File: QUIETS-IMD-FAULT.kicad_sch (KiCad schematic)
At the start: 7 parts, among them K1 Relay_DPDT, K2 Relay_SPDT, K3 Relay_DPDT, Q1 NMOS

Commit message: Version 2
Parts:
- removed K3: Relay_DPDT, symbol Relay:Relay_DPDT
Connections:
- net +12V: no longer K1.11
- net GND: now also K1.11
- net IMD FAULT LIGHT: now also K1.22
- net IMD SAFETY RELAY: now reaches K1.14
- net RESET renamed IMD-RESET
- no-connect marks 3 -> 2
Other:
- note added: "Lors de l'activation du vehicule, il faut reset l'erreur pour activer le circuit"
- moved on the sheet: K1, K2, Q1, R1, R2, R3

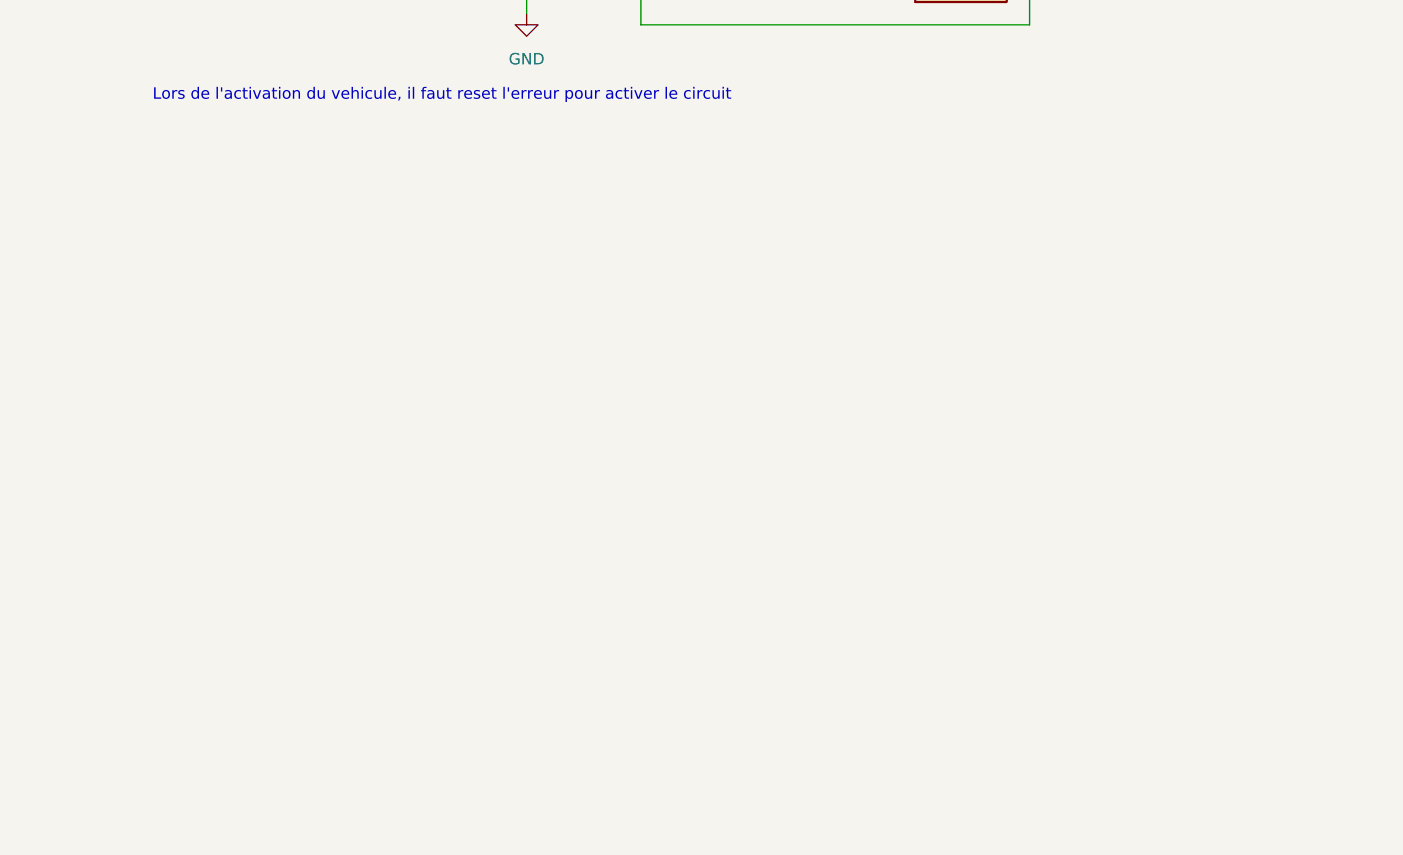
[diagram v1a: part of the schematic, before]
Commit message: Ajout BMS latch
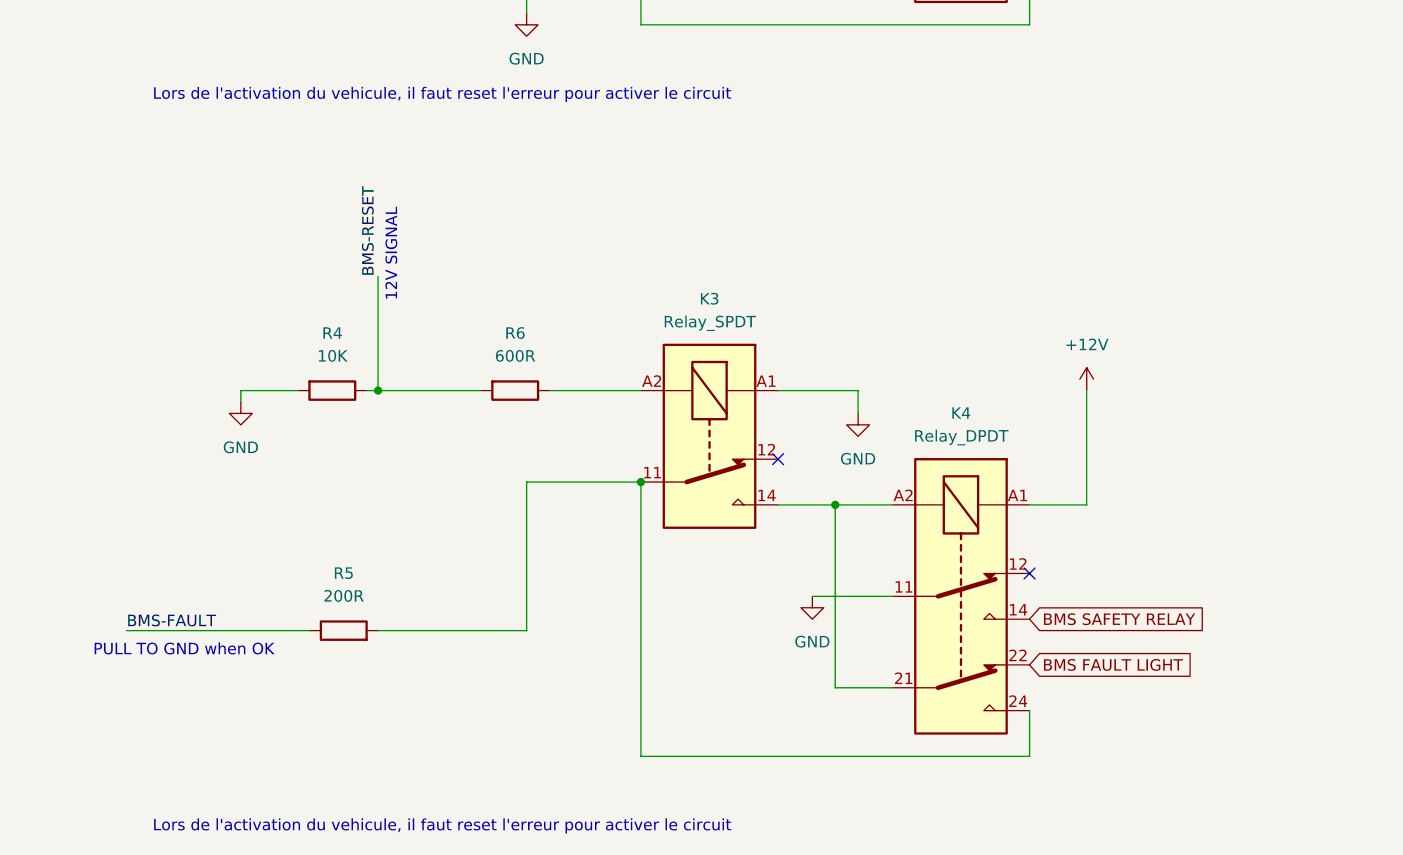
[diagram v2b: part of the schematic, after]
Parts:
- added K3: Relay_SPDT, symbol Relay:Relay_SPDT
- added K4: Relay_DPDT, symbol Relay:Relay_DPDT
- added R4: 10K, symbol Device:R
- added R5: 200R, symbol Device:R
- added R6: 600R, symbol Device:R
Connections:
- net +12V: now also K4.A1
- net GND: now also K3.A1, K4.11, R4.2
- new net: K3.A2, R6.1
- new net: K3.11, K4.24, R5.2
- new net: K3.14, K4.21, K4.A2
- new net BMS FAULT LIGHT: K4.22
- new net BMS SAFETY RELAY: K4.14
- new net BMS-FAULT: R5.1
- new net BMS-RESET: R4.1, R6.2
- no-connect marks 2 -> 4
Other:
- note added: "PULL TO GND when OK"

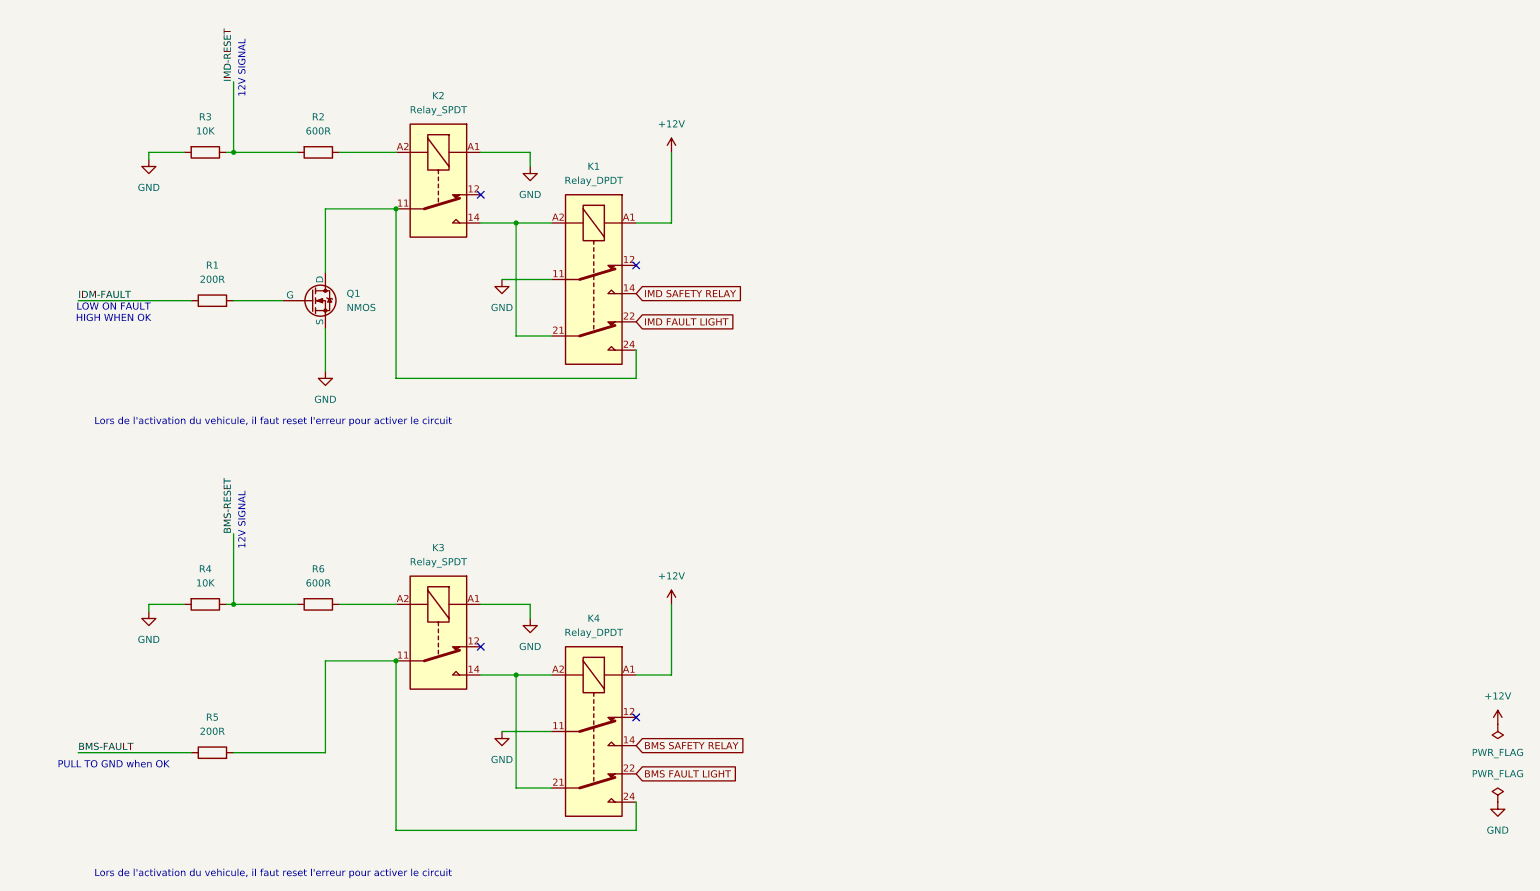
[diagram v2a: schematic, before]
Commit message: Simplification circuit IMD
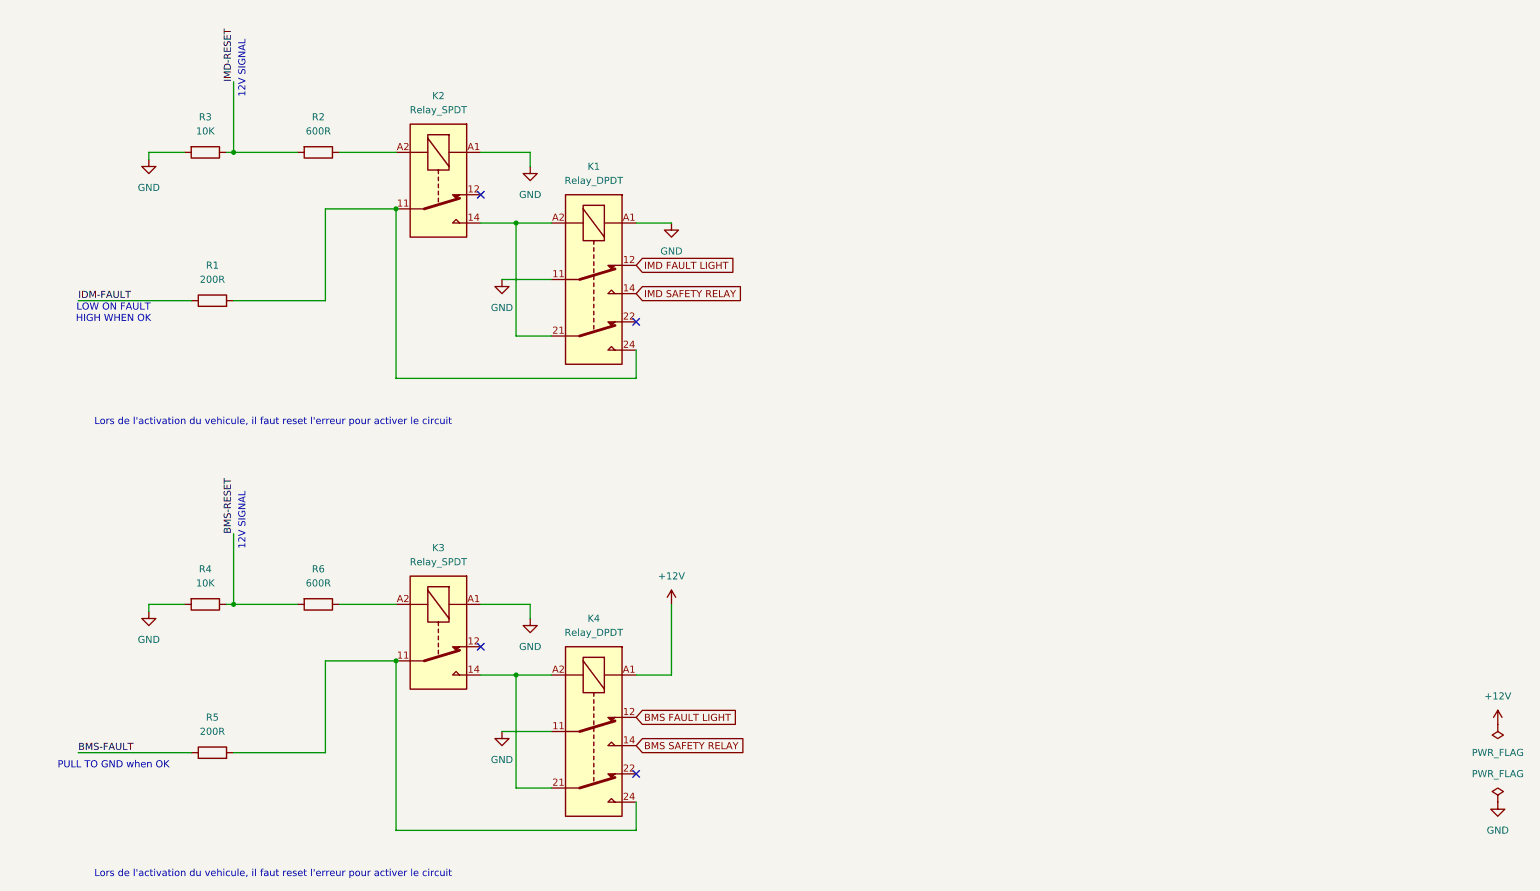
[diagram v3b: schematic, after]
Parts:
- removed Q1: NMOS, symbol Simulation_SPICE:NMOS
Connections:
- net +12V: no longer K1.A1
- net BMS FAULT LIGHT: now also K4.12; no longer K4.22
- net GND: now also K1.A1
- net IMD FAULT LIGHT: now also K1.12; no longer K1.22
- net at K1.24, K2.11: now also R1.2
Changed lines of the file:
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@@
 	)
 	(no_connect
-		(at 121.92 59.69)
+		(at 121.92 69.85)
 	)
 	(no_connect
-		(at 121.92 140.97)
+		(at 121.92 151.13)
 	)
 	(no_connect
@@
 	(wire
 		(pts
-			(xy 66.04 49.53) (xy 66.04 60.96)
-		)
-		(stroke
-			(width 0)
-			(type default)
-		)
-	)
-	(wire
-		(pts
 			(xy 49.53 107.95) (xy 49.53 120.65)
 		)
@@
 	(wire
 		(pts
+			(xy 66.04 49.53) (xy 66.04 66.04)
+		)
+		(stroke
+			(width 0)
+			(type default)
+		)
+	)
+	(wire
+		(pts
 			(xy 21.59 66.04) (xy 41.91 66.04)
 		)
@@
 	(wire
 		(pts
-			(xy 66.04 71.12) (xy 66.04 78.74)
-		)
-		(stroke
-			(width 0)
-			(type default)
-		)
-	)
-	(wire
-		(pts
 			(xy 100.33 133.35) (xy 106.68 133.35)
 		)
@@
 	(wire
 		(pts
-			(xy 128.27 52.07) (xy 128.27 39.37)
-		)
-		(stroke
-			(width 0)
-			(type default)
-		)
-	)
-	(wire
-		(pts
 			(xy 121.92 52.07) (xy 128.27 52.07)
 		)
@@
 	(wire
 		(pts
-			(xy 49.53 66.04) (xy 58.42 66.04)
+			(xy 49.53 66.04) (xy 66.04 66.04)
 		)
 		(stroke
@@
 		)
 	)
-	(global_label "BMS FAULT LIGHT"
+	(global_label "IMD FAULT LIGHT"
 		(shape input)
-		(at 121.92 151.13 0)
+		(at 121.92 59.69 0)
 		(fields_autoplaced yes)
 		(effects
@@
 		)
 		(property "Intersheetrefs" "${INTERSHEET_REFS}"
-			(at 140.871 151.13 0)
+			(at 140.871 59.69 0)
 			(effects
 				(font
@@
 		)
 	)
+	(global_label "BMS FAULT LIGHT"
+		(shape input)
+		(at 121.92 140.97 0)
+		(fields_autoplaced yes)
+		(effects
+			(font
+				(size 1.27 1.27)
+			)
+			(justify left)
+		)
+		(property "Intersheetrefs" "${INTERSHEET_REFS}"
+			(at 140.871 140.97 0)
+			(effects
+				(font
+					(size 1.27 1.27)
+				)
+				(justify left)
+				(hide yes)
+			)
+		)
+	)
 	(global_label "IMD SAFETY RELAY"
 		(shape input)
@@
 		(property "Intersheetrefs" "${INTERSHEET_REFS}"
 			(at 142.3828 64.77 0)
-			(effects
-				(font
-					(size 1.27 1.27)
-				)
-				(justify left)
-				(hide yes)
-			)
-		)
-	)
-	(global_label "IMD FAULT LIGHT"
-		(shape input)
-		(at 121.92 69.85 0)
-		(fields_autoplaced yes)
-		(effects
-			(font
-				(size 1.27 1.27)
-			)
-			(justify left)
-		)
-		(property "Intersheetrefs" "${INTERSHEET_REFS}"
-			(at 140.871 69.85 0)
 			(effects
 				(font
@@
 	)
 	(symbol
-		(lib_id "Simulation_SPICE:NMOS")
-		(at 63.5 66.04 0)
-		(unit 1)
-		(exclude_from_sim no)
-		(in_bom yes)
-		(on_board yes)
-		(dnp no)
-		(fields_autoplaced yes)
-		(property "Reference" "Q1"
-			(at 69.85 64.7699 0)
-			(effects
-				(font
-					(size 1.27 1.27)
-				)
-				(justify left)
-			)
-		)
-		(property "Value" "NMOS"
-			(at 69.85 67.3099 0)
-			(effects
-				(font
-					(size 1.27 1.27)
-				)
-				(justify left)
-			)
-		)
-		(property "Footprint" ""
-			(at 68.58 63.5 0)
-			(effects
-				(font
-					(size 1.27 1.27)
-				)
-				(hide yes)
-			)
-		)
-		(property "Datasheet" "https://ngspice.sourceforge.io/docs/ngspice-html-manual/manual.xhtml#cha_MOSFETs"
-			(at 63.5 78.74 0)
-			(effects
-				(font
-					(size 1.27 1.27)
-				)
-				(hide yes)
-			)
-		)
-		(property "Description" "N-MOSFET transistor, drain/source/gate"
-			(at 63.5 66.04 0)
-			(effects
-				(font
-					(size 1.27 1.27)
-				)
-				(hide yes)
-			)
-		)
-		(property "Sim.Device" "NMOS"
-			(at 63.5 83.185 0)
-			(effects
-				(font
-					(size 1.27 1.27)
-				)
-				(hide yes)
-			)
-		)
-		(property "Sim.Type" "VDMOS"
-			(at 63.5 85.09 0)
-			(effects
-				(font
-					(size 1.27 1.27)
-				)
-				(hide yes)
-			)
-		)
-		(property "Sim.Pins" "1=D 2=G 3=S"
-			(at 63.5 81.28 0)
-			(effects
-				(font
-					(size 1.27 1.27)
-				)
-				(hide yes)
-			)
-		)
-		(pin "1"
-		)
-		(pin "3"
-		)
-		(pin "2"
-		)
-		(instances
-			(project ""
-				(path "/ed7753a8-1a5c-4fe4-806d-46e20e917c92"
-					(reference "Q1")
-					(unit 1)
-				)
-			)
-		)
-	)
-	(symbol
 		(lib_id "Device:R")
 		(at 64.77 120.65 270)
@@
 	)
 	(symbol
-		(lib_id "power:+12V")
-		(at 128.27 39.37 0)
-		(unit 1)
-		(exclude_from_sim no)
-		(in_bom yes)
-		(on_board yes)
-		(dnp no)
-		(fields_autoplaced yes)
-		(property "Reference" "#PWR01"
-			(at 128.27 43.18 0)
-			(effects
-				(font
-					(size 1.27 1.27)
-				)
-				(hide yes)
-			)
-		)
-		(property "Value" "+12V"
-			(at 128.27 34.29 0)
-			(effects
-				(font
-					(size 1.27 1.27)
-				)
-			)
-		)
-		(property "Footprint" ""
-			(at 128.27 39.37 0)
-			(effects
-				(font
-					(size 1.27 1.27)
-				)
-				(hide yes)
-			)
-		)
-		(property "Datasheet" ""
-			(at 128.27 39.37 0)
-			(effects
-				(font
-					(size 1.27 1.27)
-				)
-				(hide yes)
-			)
-		)
-		(property "Description" "Power symbol creates a global label with name \"+12V\""
-			(at 128.27 39.37 0)
-			(effects
-				(font
-					(size 1.27 1.27)
-				)
-				(hide yes)
-			)
-		)
-		(pin "1"
-		)
-		(instances
-			(project ""
-				(path "/ed7753a8-1a5c-4fe4-806d-46e20e917c92"
-					(reference "#PWR01")
-					(unit 1)
-				)
-			)
-		)
-	)
-	(symbol
 		(lib_id "Relay:Relay_SPDT")
 		(at 86.36 125.73 270)
@@
 	(symbol
 		(lib_id "power:GND")
+		(at 128.27 52.07 0)
+		(unit 1)
+		(exclude_from_sim no)
+		(in_bom yes)
+		(on_board yes)
+		(dnp no)
+		(fields_autoplaced yes)
+		(property "Reference" "#PWR01"
+			(at 128.27 58.42 0)
+			(effects
+				(font
+					(size 1.27 1.27)
+				)
+				(hide yes)
+			)
+		)
+		(property "Value" "GND"
+			(at 128.27 57.15 0)
+			(effects
+				(font
+					(size 1.27 1.27)
+				)
+			)
+		)
+		(property "Footprint" ""
+			(at 128.27 52.07 0)
+			(effects
+				(font
+					(size 1.27 1.27)
+				)
+				(hide yes)
+			)
+		)
+		(property "Datasheet" ""
+			(at 128.27 52.07 0)
+			(effects
+				(font
+					(size 1.27 1.27)
+				)
+				(hide yes)
+			)
+		)
+		(property "Description" "Power symbol creates a global label with name \"GND\" , ground"
+			(at 128.27 52.07 0)
+			(effects
+				(font
+					(size 1.27 1.27)
+				)
+				(hide yes)
+			)
+		)
+		(pin "1"
+		)
+		(instances
+			(project "QUIETS-IMD-FAULT"
+				(path "/ed7753a8-1a5c-4fe4-806d-46e20e917c92"
+					(reference "#PWR01")
+					(unit 1)
+				)
+			)
+		)
+	)
+	(symbol
+		(lib_id "power:GND")
 		(at 34.29 40.64 0)
 		(unit 1)
@@
 					(unit 1)
 				)
-			)
-		)
-	)
-	(symbol
-		(lib_id "power:GND")
-		(at 66.04 78.74 0)
-		(unit 1)
-		(exclude_from_sim no)
-		(in_bom yes)
-		(on_board yes)
-		(dnp no)
-		(fields_autoplaced yes)
-		(property "Reference" "#PWR02"
-			(at 66.04 85.09 0)
-			(effects
-				(font
-					(size 1.27 1.27)
-				)
-				(hide yes)
-			)
-		)
-		(property "Value" "GND"
-			(at 66.04 83.82 0)
-			(effects
-				(font
-					(size 1.27 1.27)
-				)
-			)
-		)
-		(property "Footprint" ""
-			(at 66.04 78.74 0)
-			(effects
-				(font
-					(size 1.27 1.27)
-				)
-				(hide yes)
-			)
-		)
-		(property "Datasheet" ""
-			(at 66.04 78.74 0)
-			(effects
-				(font
-					(size 1.27 1.27)
-				)
-				(hide yes)
-			)
-		)
-		(property "Description" "Power symbol creates a global label with name \"GND\" , ground"
-			(at 66.04 78.74 0)
-			(effects
-				(font
-					(size 1.27 1.27)
-				)
-				(hide yes)
-			)
-		)
-		(pin "1"
-		)
-		(instances
-			(project ""
-				(path "/ed7753a8-1a5c-4fe4-806d-46e20e917c92"
-					(reference "#PWR02")
-					(unit 1)
-				)
